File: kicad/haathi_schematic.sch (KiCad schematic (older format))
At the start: 0 parts

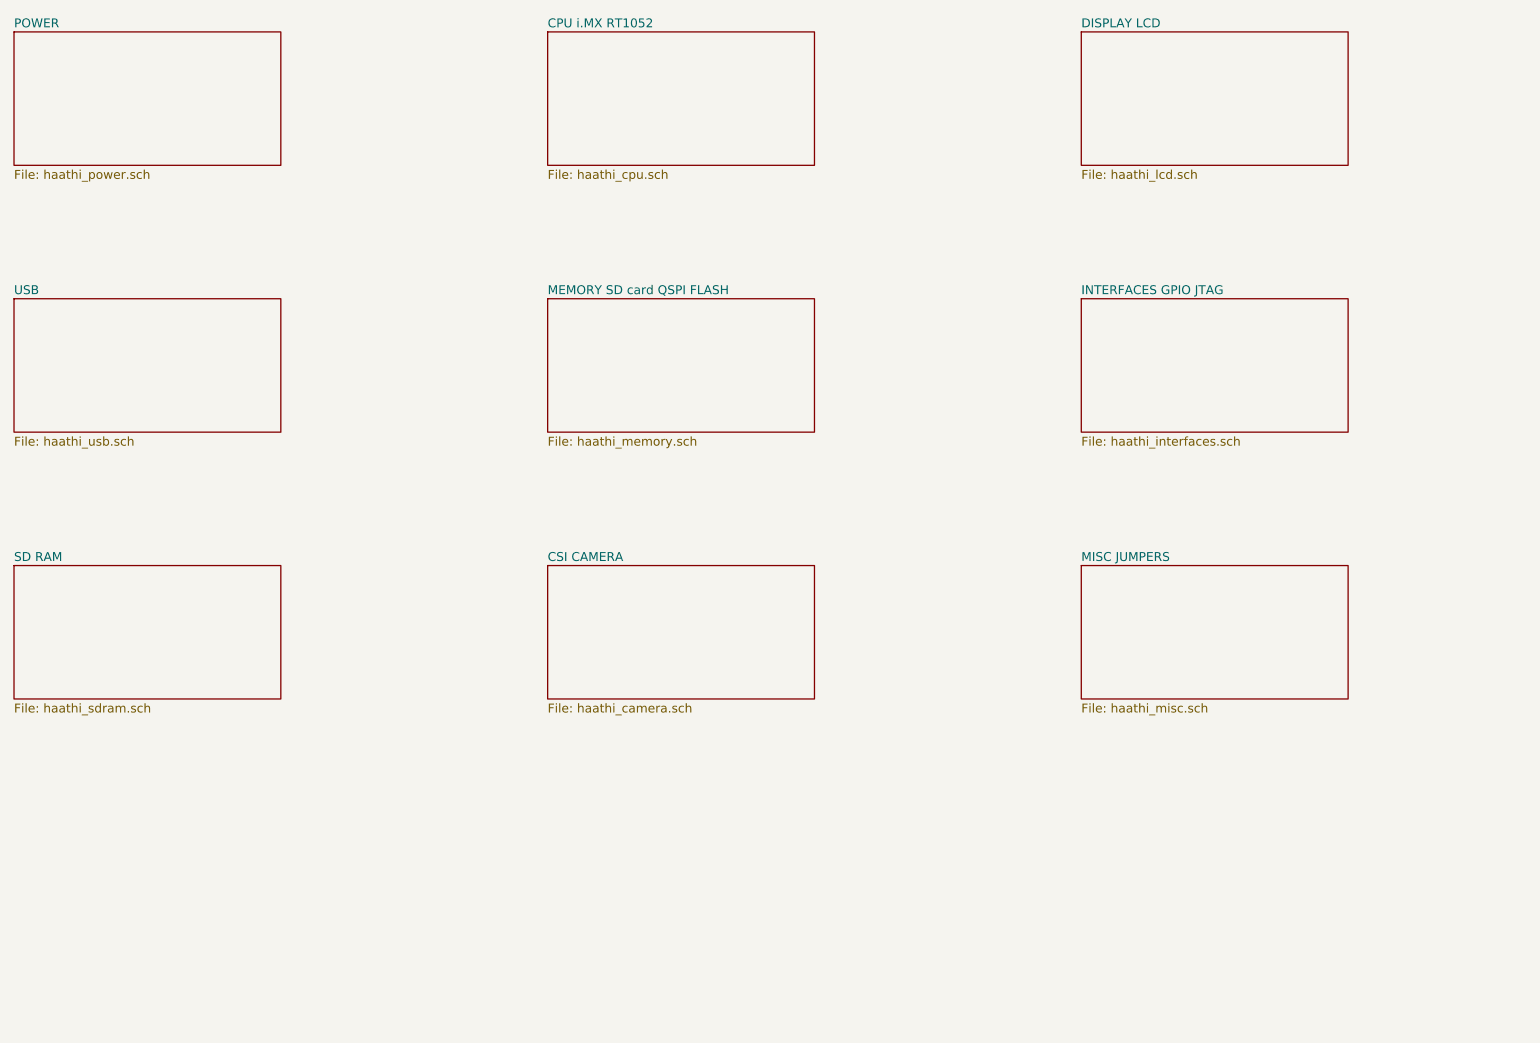
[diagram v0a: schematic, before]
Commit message: created schematic structure
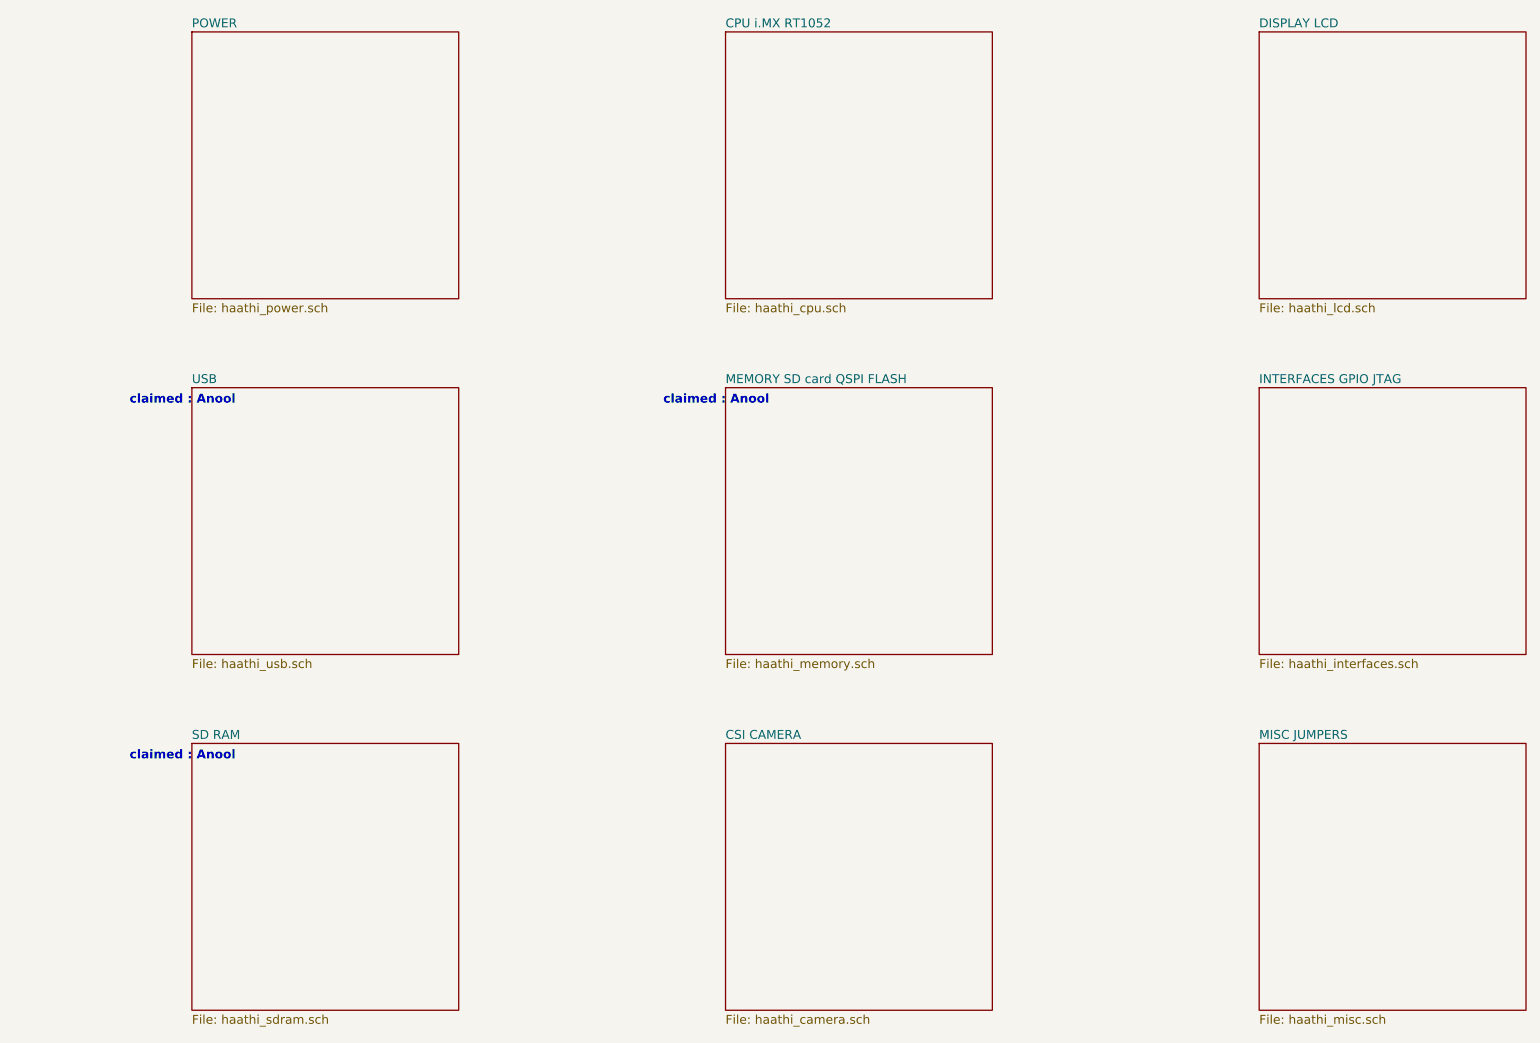
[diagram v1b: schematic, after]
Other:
- note added: "claimed : Anool"
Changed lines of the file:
@@
 $Descr A4 11693 8268
 encoding utf-8
-Sheet 3 11
+Sheet 3 12
 Title ""
 Date ""
@@
 $EndDescr
 $Sheet
-S 1000 1000 1500 750
+S 2000 1000 1500 1500
 U 5A630787
 F0 "POWER" 50
@@
 $EndSheet
 $Sheet
-S 4000 1000 1500 750
+S 5000 1000 1500 1500
 U 5A6307C3
 F0 "CPU i.MX RT1052" 50
@@
 $EndSheet
 $Sheet
-S 7000 1000 1500 750
+S 8000 1000 1500 1500
 U 5A6307F7
 F0 "DISPLAY LCD" 50
@@
 $EndSheet
 $Sheet
-S 4000 2500 1500 750
+S 5000 3000 1500 1500
 U 5A63081E
 F0 "MEMORY SD card QSPI FLASH" 50
@@
 $EndSheet
 $Sheet
-S 1000 2500 1500 750
+S 2000 3000 1500 1500
 U 5A630892
 F0 "USB" 50
@@
 $EndSheet
 $Sheet
-S 7000 2500 1500 750
+S 8000 3000 1500 1500
 U 5A6308C3
 F0 "INTERFACES GPIO JTAG" 50
@@
 $EndSheet
 $Sheet
-S 1000 4000 1500 750
+S 2000 5000 1500 1500
 U 5A6308E9
 F0 "SD RAM" 50
@@
 $EndSheet
 $Sheet
-S 4000 4000 1500 750
+S 5000 5000 1500 1500
 U 5A630911
 F0 "CSI CAMERA" 50
@@
 $EndSheet
 $Sheet
-S 7000 4000 1500 750
+S 8000 5000 1500 1500
 U 5A630933
 F0 "MISC JUMPERS" 50
 F1 "haathi_misc.sch" 50
 $EndSheet
+Text Notes 1650 3100 0    50   ~ 10
+claimed : Anool
+Text Notes 1650 5100 0    50   ~ 10
+claimed : Anool
+Text Notes 4650 3100 0    50   ~ 10
+claimed : Anool
 $EndSCHEMATC

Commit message: Claimed sheets and cloned schem sym lib
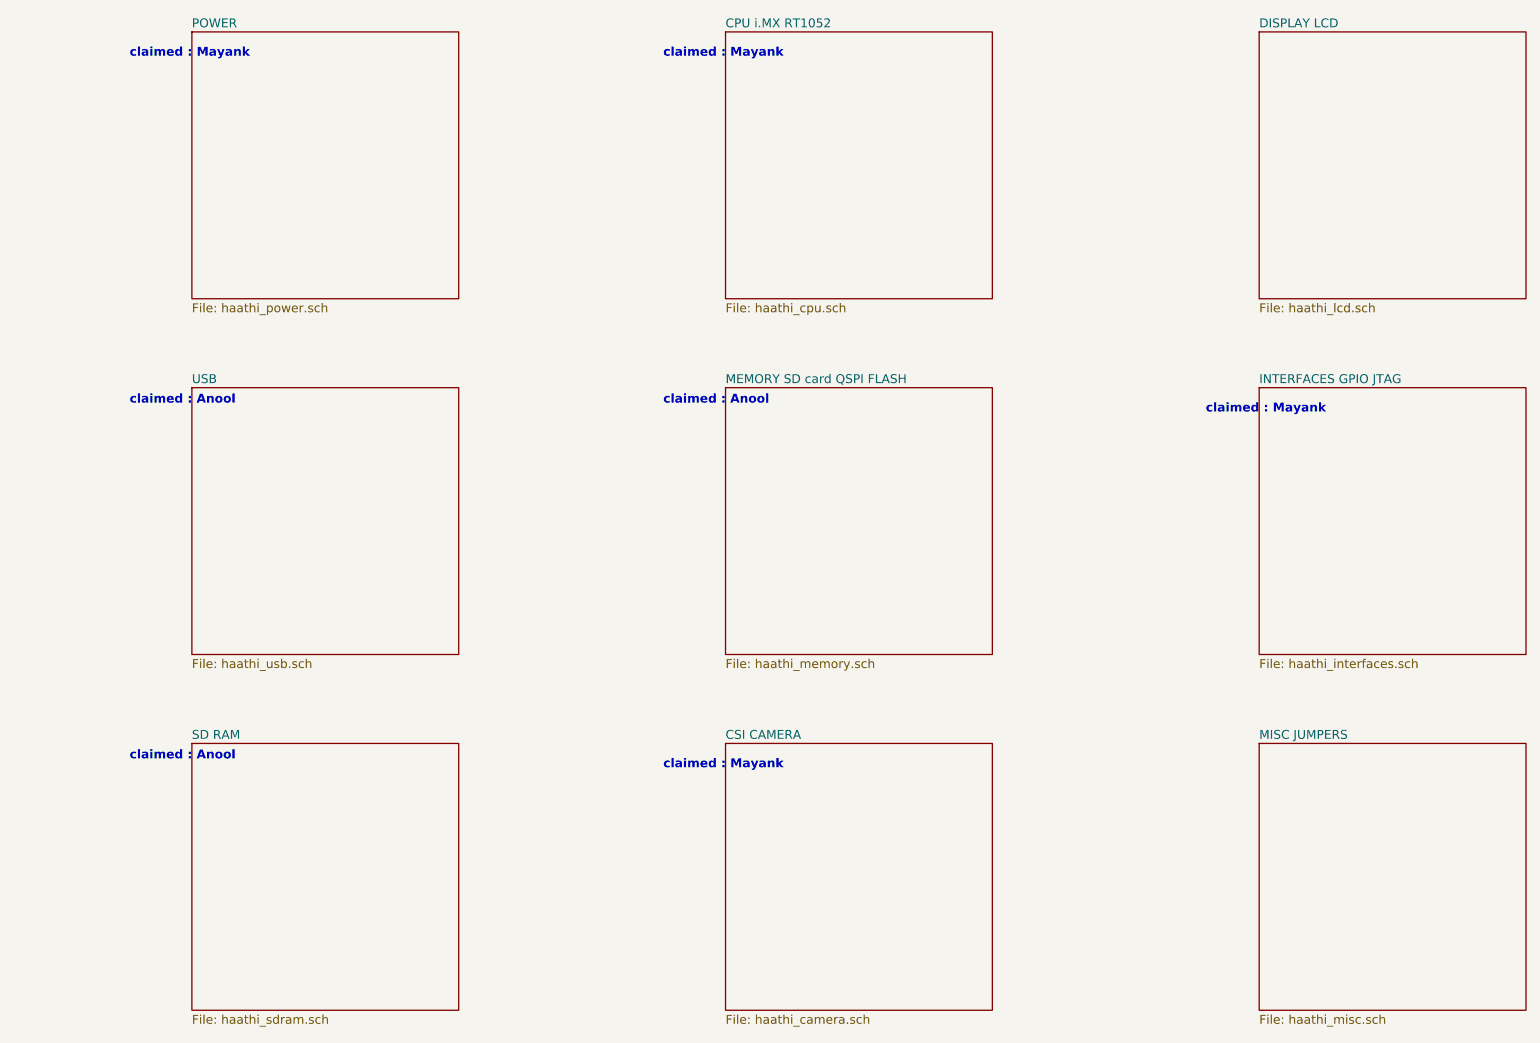
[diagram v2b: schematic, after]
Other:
- note added: "claimed : Mayank"
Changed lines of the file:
@@
 Text Notes 4650 3100 0    50   ~ 10
 claimed : Anool
+Text Notes 1650 1150 0    50   ~ 10
+claimed : Mayank
+Text Notes 4650 5150 0    50   ~ 10
+claimed : Mayank
+Text Notes 4650 1150 0    50   ~ 10
+claimed : Mayank
+Text Notes 7700 3150 0    50   ~ 10
+claimed : Mayank
 $EndSCHEMATC

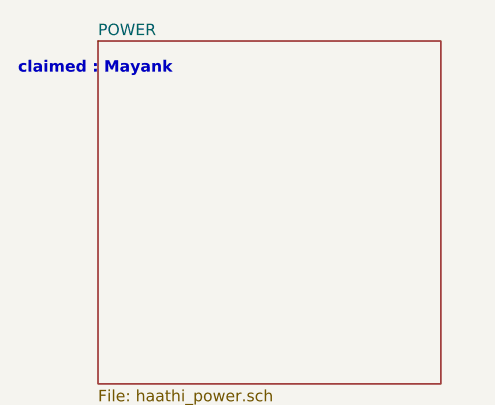
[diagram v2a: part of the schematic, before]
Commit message: Added power circuits for buck converter and snvs
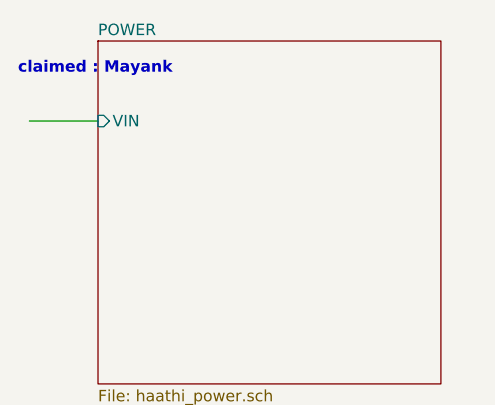
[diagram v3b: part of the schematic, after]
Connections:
- wire segments 0 -> 1
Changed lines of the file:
@@
 F0 "POWER" 50
 F1 "haathi_power.sch" 50
+F2 "VIN" I L 2000 1350 50
 $EndSheet
 $Sheet
@@
 Text Notes 7700 3150 0    50   ~ 10
 claimed : Mayank
+Wire Wire Line
+	2000 1350 1700 1350
 $EndSCHEMATC
